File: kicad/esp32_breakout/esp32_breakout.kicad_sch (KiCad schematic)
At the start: 26 parts, among them J1 JST B5B-PH-K-S, J10 JST B6B-PH-K-S, J2 JST B5B-PH-K-S, J3 JST B7B-PH-K-S, J4 XT30U-M, J5 HDR F 2.54MM VERT, J6 HDR F 2.54MM 5-pin VERT, J9 JST B6B-PH-K-S, SW1 SS12D10, U1 ESP32 DEV KIT Module 30-pin, U2 LM2596 Module

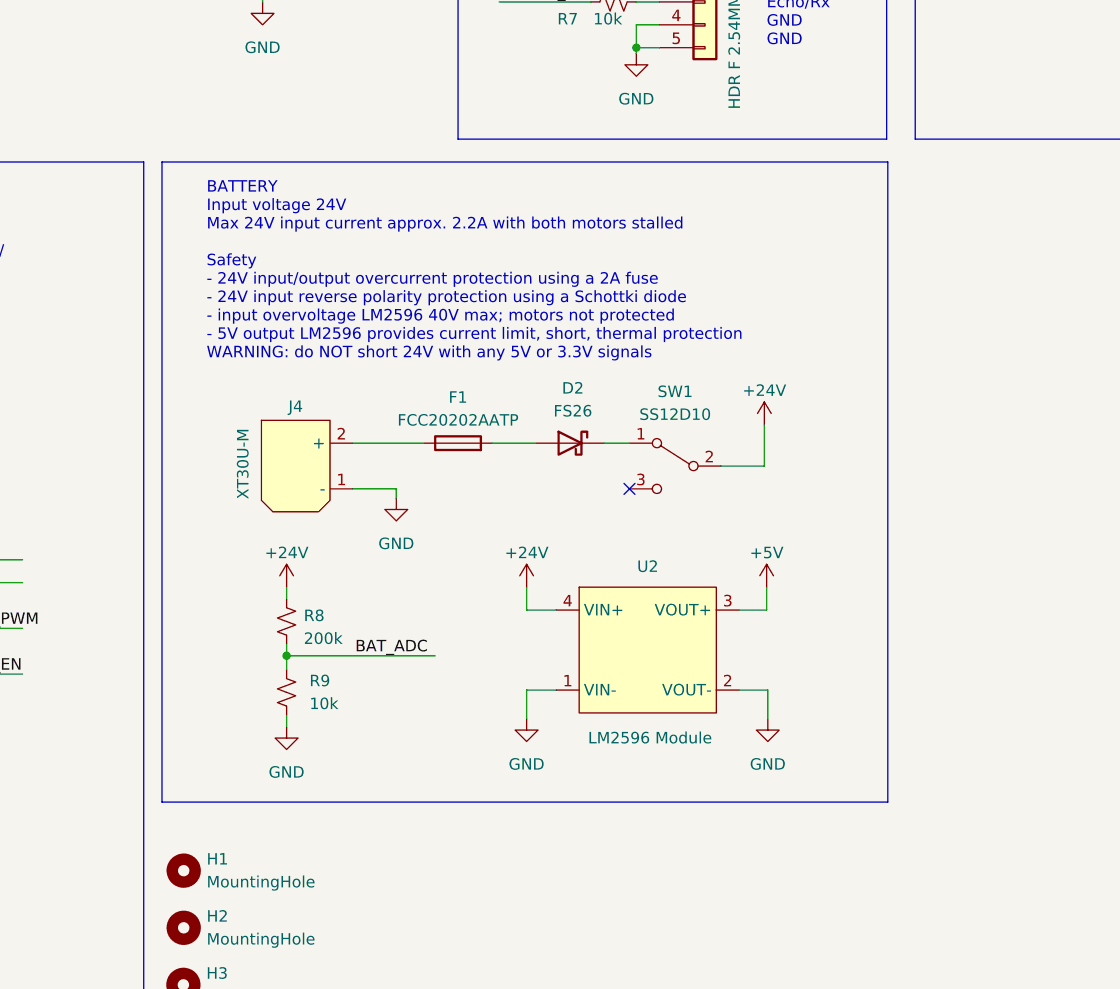
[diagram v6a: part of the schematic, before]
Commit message: Alt fuse; fan fix
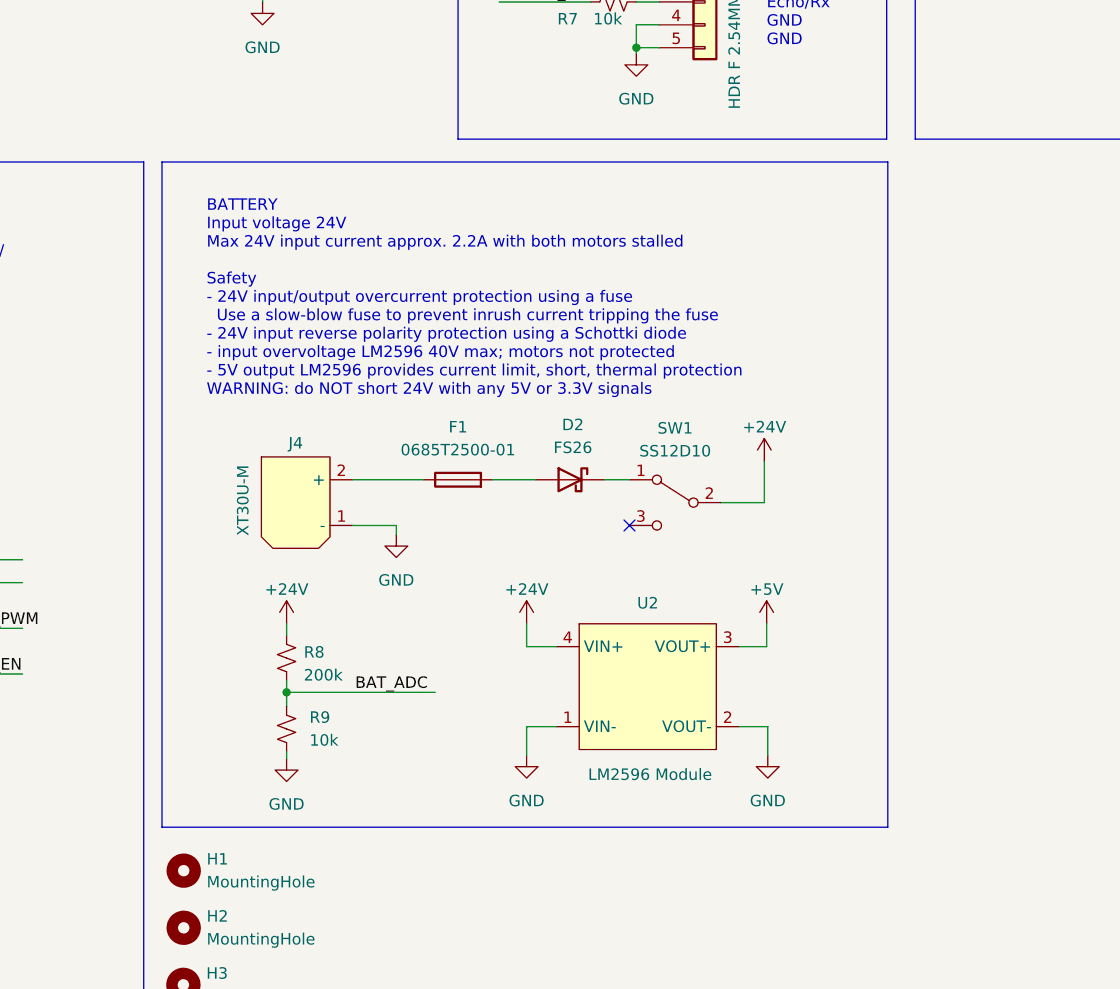
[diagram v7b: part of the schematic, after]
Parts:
- F1: value FCC20202AATP -> 0685T2500-01; footprint Fuse:Fuse_0805_2012Metric -> Fuse:Fuse_1206_3216Metric
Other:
- note added: "BATTERY Input voltage 24V Max 24V input current approx. 2.2A with both motors stalled Safety - 24V input/output overcurrent protection using a fuse Use a slow-blow fuse to prevent inrush current tripping the fuse - 24V input reverse polarity protection using a Schottki diode - input overvoltage LM2596 40V max; motors not protected - 5V output LM2596 provides current limit, short, thermal protecti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"
- note removed: "BATTERY Input voltage 24V Max 24V input current approx. 2.2A with both motors stalled Safety - 24V input/output overcurrent protection using a 2A fuse - 24V input reverse polarity protection using a Schottki diode - input overvoltage LM2596 40V max; motors not protected - 5V output LM2596 provides current limit, short, thermal protection WARNING: do NOT short 24V with any 5V or 3.3V signals"
- moved on the sheet: D2, F1, J4, R8, R9, SW1, U2

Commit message: ESP32 PCB v1.1.0
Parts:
- J5: value HDR F 2.54MM VERT -> HDR 8p M VERT 2.54mm; footprint Connector_PinSocket_2.54mm:PinSocket_1x08_P2.54mm_Vertical -> Connector_PinHeader_2.54mm:PinHeader_1x08_P2.54mm_Vertical
- J6: value HDR F 2.54MM 5-pin VERT -> JST B5B-ZR; footprint Connector_PinSocket_2.54mm:PinSocket_1x05_P2.54mm_Vertical -> Makerspet:JST_ZH_B5B-ZR_1x05_P1.50mm_Vertical
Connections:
- net LDS_MOT_EN renamed LDS_EN
